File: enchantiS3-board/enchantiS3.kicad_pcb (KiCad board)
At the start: 4 copper layers, 55.9 x 25.4 mm, 60 parts, among them J1 USB_C_Receptacle_USB2.0, SW1 B3U-1000P, SW2 B3U-1000P, U1 USBLC6-2P6, U10 BQ25185DLHR, U3 NCV8187AMT330TAG, U4 NCV8187AMT330TAG, U6 MAX17262REWL+T, U7 LSM6DSV16XTR, U8 IIS2MDCTR

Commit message: added CIRMMT logo to silkscreen
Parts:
- added G***: LOGO, logos:CIRMMT_logo, B.Cu at (135.2, 60.2)
- moved G*** 31.5 mm to (103.9, 51.2)

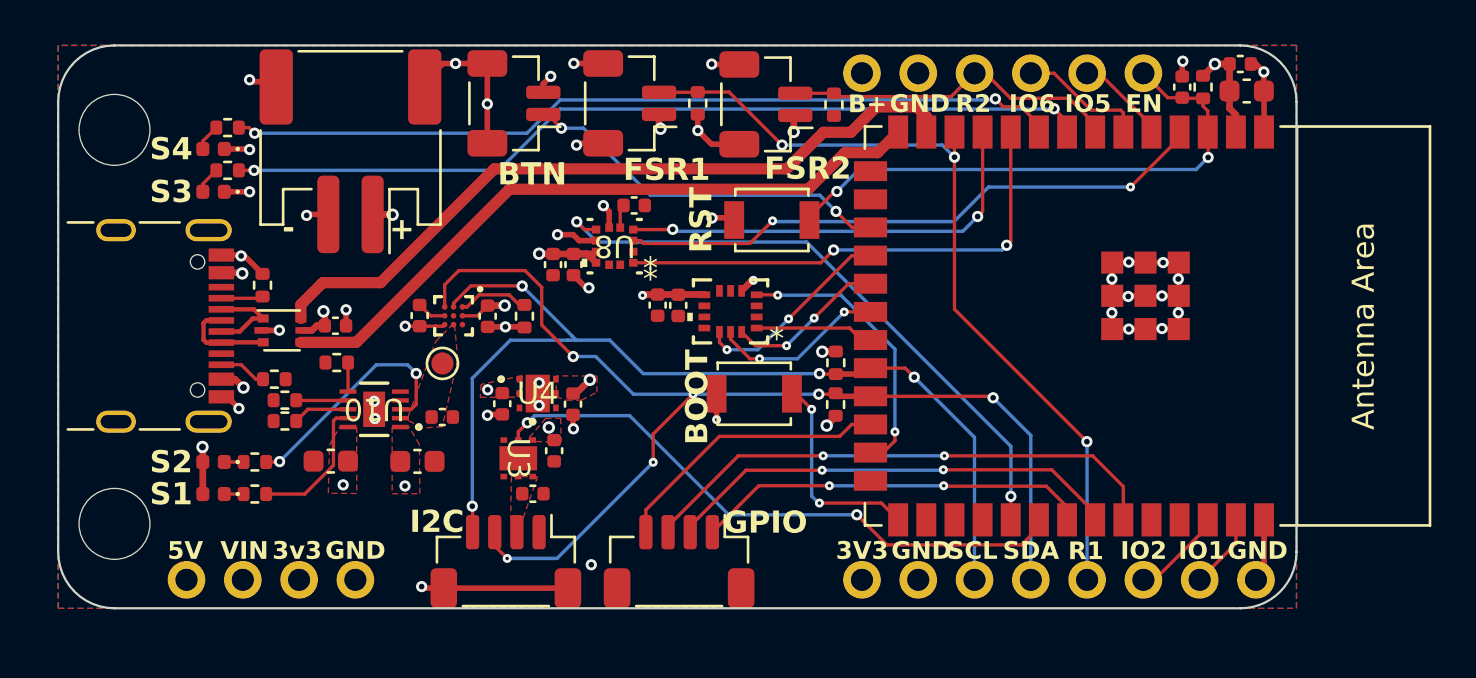
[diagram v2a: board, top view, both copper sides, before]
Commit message: finsished routing for revision 4 of enchantiS3, finished routing for  enchantiS3 Touch
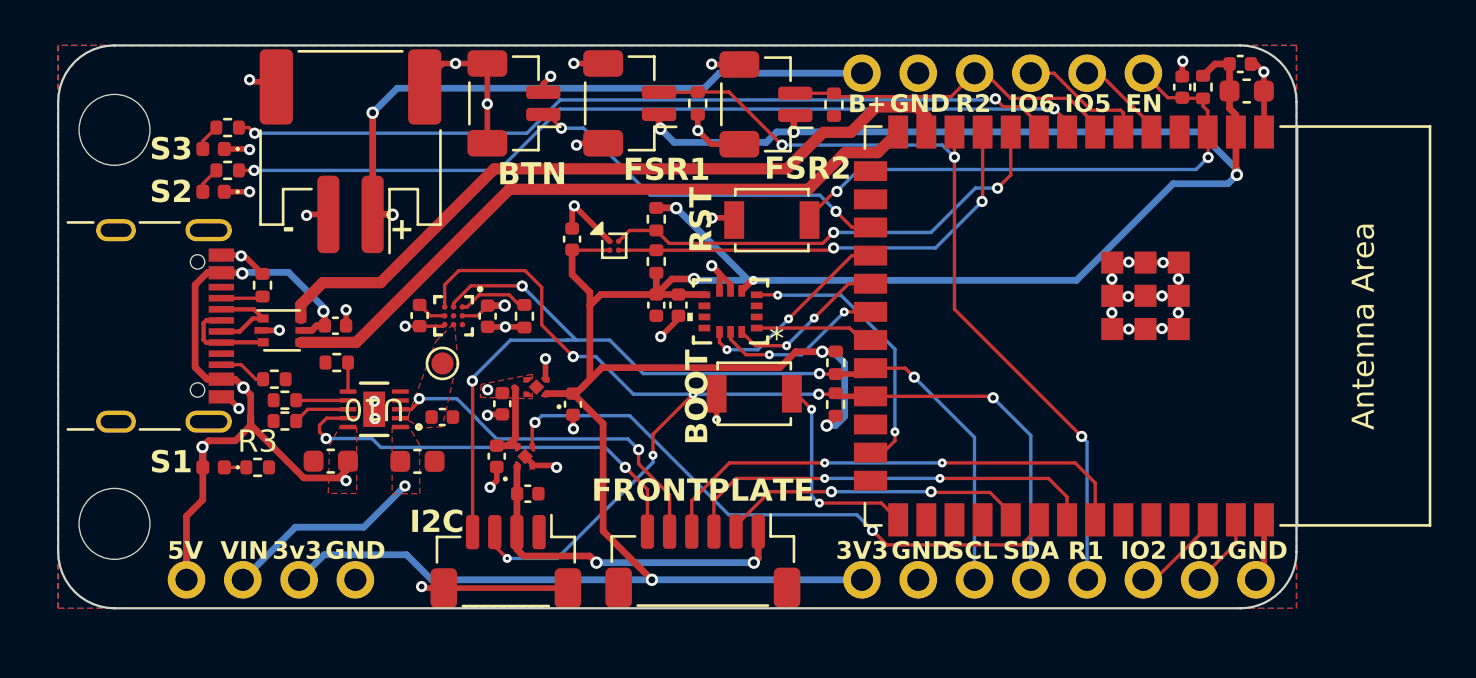
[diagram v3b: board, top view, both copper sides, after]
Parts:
- removed C10: 1uF, Capacitor_SMD:C_0402_1005Metric
- removed C18: 220nF, Capacitor_SMD:C_0402_1005Metric
- removed C7: 0.1uF, Capacitor_SMD:C_0402_1005Metric
- removed CHARGLED2: S2, LED_SMD:LED_0402_1005Metric
- removed R22: 1k, Resistor_SMD:R_0402_1005Metric
- removed TOUCH2: JST-SH-1x04 1.0mm, Connector_JST:JST_SH_BM04B-SRSS-TB_1x04-1MP_P1.00mm_Vertical
- removed U3, U4: NCV8187AMT330TAG, NCV8187-footprints:NCV8187AMT330TAG_ONS-L
- added C3: 220nF, Capacitor_SMD:C_0402_1005Metric, F.Cu at (115.9, 57.0)
- added FP1: JST-SH-1x04 1.0mm, Connector_JST:JST_SH_BM06B-SRSS-TB_1x06-1MP_P1.00mm_Vertical, F.Cu at (121.8, 71.5)
- added R4: 2k2, Resistor_SMD:R_0402_1005Metric, F.Cu at (119.7, 56.1)
- added R9: 2k2, Resistor_SMD:R_0402_1005Metric, F.Cu at (119.7, 58.0)
- added U2: MMC5633NJL, Package_BGA:WLP-4_0.86x0.86mm_P0.4mm, F.Cu at (117.8, 57.3)
- added U5: NCP167AMX330TBG, NCP167AMX330TBG-footprints:XDFN4_1X1_711AJ_ONS, F.Cu at (114.3, 63.7)
- R1, R2: value 1k -> 10k
- R3: value 1k -> 2k2
- U8: value IIS2MDCTR -> NCP167AMX330TBG; footprint IIS2MDCTR-footprints:LGA-12_2X2X0P7_STM -> NCP167AMX330TBG-footprints:XDFN4_1X1_711AJ_ONS
- moved U8 10.3 mm to (113.8, 66.8), turned to 90 degrees
- moved C20 5.95 mm to (120.7, 60.0)
- moved C6 4.16 mm to (119.7, 60.0)
- moved C4 2.60 mm to (112.5, 66.8)
- moved R3 1.21 mm to (101.7, 67.3)
- moved CHARGLED1 1.20 mm to (99.7, 67.3)
- moved C5 0.23 mm to (113.9, 68.5)
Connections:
- MCU1 pad 10: /SPC -> /SCL2
- MCU1 pad 11: /SDIO -> /SDA2
- MCU1 pad 24: /EVT4 -> /LED4
- MCU1 pad 31: /MAG_INT -> /BTN_FP
- MCU1 pad 33: /EVT1 -> /LED1
- MCU1 pad 34: /EVT2 -> /LED2
- MCU1 pad 35: /EVT3 -> /LED3
- MCU1 pad 4: /CS1 -> unconnected-(MCU1-GPIO4/TOUCH4/ADC1_CH3-Pad4)
- R3 pad 2: /STAT1 -> GND
- U8 pad 1: /SPC -> 3V3_AUX
- U8 pad 2: unconnected-(U8-NC-Pad2) -> GND
- U8 pad 3: /CS1 -> /LDO_EN
- U8 pad 4: /SDIO -> SYS
- U8 pad 5: Net-(U8-C1) -> GND
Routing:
- net +3V3: track 15.6 -> 140.4 mm
- net /MAG_INT: track 28.1 -> 0.00 mm, vias 2 -> 0
- net +BATT: track 3.01 -> 30.4 mm, vias 2 -> 3
- net /CS1: track 27.0 -> 0.00 mm, vias 2 -> 0
- net VUSB: track 6.01 -> 32.8 mm
- net /EVT3: track 24.2 -> 0.00 mm, vias 2 -> 0
- net /SPC: track 22.4 -> 0.00 mm, vias 2 -> 0
- net /LED2: track 0.00 -> 22.3 mm, vias 0 -> 2
- net /SCL2: track 0.00 -> 21.4 mm, vias 0 -> 2
- net /EVT2: track 20.7 -> 0.00 mm, vias 2 -> 0
- net /SDA2: track 0.00 -> 20.5 mm, vias 0 -> 2
- net /SDIO: track 19.8 -> 0.00 mm, vias 2 -> 0
- net /LED1: track 0.00 -> 19.1 mm, vias 0 -> 2
- net /EVT1: track 17.9 -> 0.00 mm, vias 2 -> 0
- net 3V3_AUX: track 0.00 -> 16.2 mm, vias 0 -> 2
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- added copper zone on In2.Cu, net GND
- removed copper zone on F.Cu, net +3V3
- removed copper zone on F.Cu, net 3V3_AUX
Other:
- board text added: "FRONTPLATE"
- board text removed: "EVT1 = GPIO40 EVT2 = GPIO41 EVT3 = GPIO42 EVT4 = GPIO47"
- board text removed: "GPIO"
- board text removed: "S4"

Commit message: updated project to kicad 8.0, switched to using enchantiLibrary footprint/symbols, switched connectors to molex picoclasp, updated imu
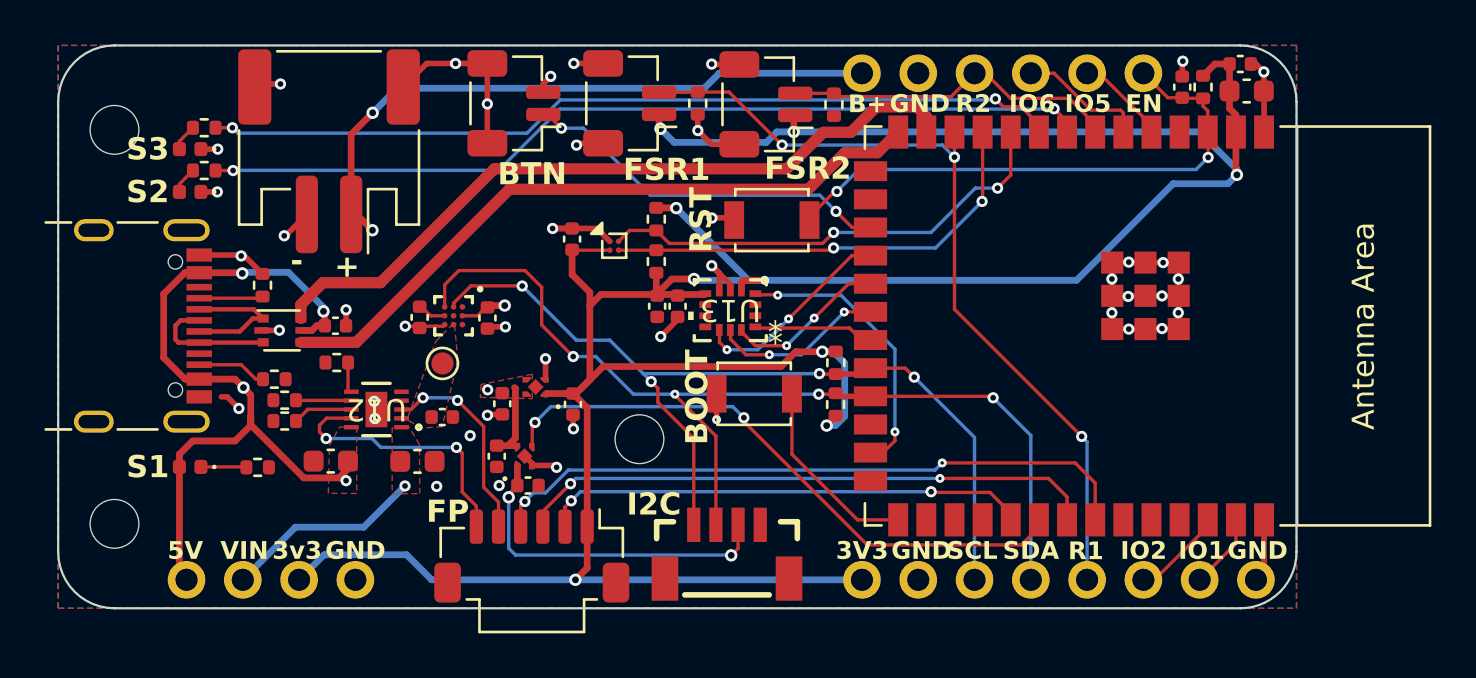
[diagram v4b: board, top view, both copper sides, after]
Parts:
- removed C1, C20: 0.1uF, Capacitor_SMD:C_0402_1005Metric
- removed C2: 0.47uF, Capacitor_SMD:C_0402_1005Metric
- removed C6: 1uF, Capacitor_SMD:C_0402_1005Metric
- removed R14: 10k, Resistor_SMD:R_0402_1005Metric
- removed R19: 0.43k, Resistor_SMD:R_0402_1005Metric
- removed R20: 13k, Resistor_SMD:R_0402_1005Metric
- removed U10: BQ25185DLHR, BQ25185-footprints:WSON10_DLH_TEX-M
- removed U5, U8: NCP167AMX330TBG, NCP167AMX330TBG-footprints:XDFN4_1X1_711AJ_ONS
- removed U6: MAX17262REWL+T, max17262-footprints:21-100221A_W91G1&plus_3_MXM
- removed U7: LSM6DSV16XTR, LSM6DSV16XTR-footprints:LGA14L_LSM6_STM
- added C17: 1uF, Capacitor_SMD:C_0402_1005Metric, F.Cu at (120.7, 60.0)
- added C18: 0.1uF, Capacitor_SMD:C_0402_1005Metric, F.Cu at (119.7, 60.0)
- added C7: 0.1uF, Capacitor_SMD:C_0402_1005Metric, F.Cu at (112.1, 60.6)
- added C8: 0.47uF, Capacitor_SMD:C_0402_1005Metric, F.Cu at (109.0, 60.5)
- added H3: MountingHole, MountingHole:MountingHole_2.2mm_M2, F.Cu at (118.9, 66.0)
- added R11: 13k, Resistor_SMD:R_0402_1005Metric, F.Cu at (102.9, 64.3)
- added R15: 0.3k, Resistor_SMD:R_0402_1005Metric, F.Cu at (102.9, 65.2)
- added U11: MAX17262REWL+T, ENCHANTI_battery-management:MAX17262, F.Cu at (110.5, 60.5)
- added U12: BQ25185DLHR, ENCHANTI_battery-management:WSON10_DLH_TEX, F.Cu at (107.1, 64.7)
- added U13: ICM-42670-P, ENCHANTI_MEMS:LGA14_2P5X3X0P91_TDK, F.Cu at (123.0, 60.2)
- added U4: NCP167AMX330TBG, ENCHANTI_regulators:XDFN4_1X1_711AJ_ONS, F.Cu at (114.3, 63.7)
- added U9: NCP167AMX330TBG, ENCHANTI_regulators:XDFN4_1X1_711AJ_ONS, F.Cu at (113.8, 66.8)
- ANG1, ANG2, ANG3: value JST-SH-1.00mm 1x2 -> CONN HEADER SMD 2POS 1MM; footprint Connector_JST:JST_SH_BM02B-SRSS-TB_1x02-1MP_P1.00mm_Vertical -> ENCHANTI_connectors:Molex_Pico-Clasp_2pin_Vertical
- FP1: value JST-SH-1x04 1.0mm -> CONN HEADER SMD 6POS 1MM; footprint Connector_JST:JST_SH_BM06B-SRSS-TB_1x06-1MP_P1.00mm_Vertical -> ENCHANTI_connectors:Molex_Pico-Clasp_501331-0607_1x06-1MP_P1.00mm_Vertical
- H1, H2: footprint MountingHole:MountingHole_3.2mm_M3_DIN965 -> MountingHole:MountingHole_2.2mm_M2
- TOUCH1: footprint Connector_JST:JST_SH_BM04B-SRSS-TB_1x04-1MP_P1.00mm_Vertical -> ENCHANTI_connectors:JST_SMD_1.0mm-4_Vertical
- moved TOUCH1 9.98 mm to (122.9, 71.4)
- moved FP1 7.72 mm to (114.1, 71.3)
- moved CHARGLED1 1.06 mm to (98.7, 67.3)
- moved R10 1.06 mm to (99.3, 52.0)
- moved R8 1.06 mm to (99.3, 53.9)
- moved STATLED1 1.06 mm to (98.7, 54.9)
- moved STATLED2 1.06 mm to (98.7, 52.9)
- moved J1 1.00 mm to (95.4, 60.9)
- moved BT1 0.97 mm to (104.9, 53.0)
- moved C5 0.37 mm to (113.9, 68.1)
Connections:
- FP1 pad 1: 3V3_AUX -> +3V3
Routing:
- net /BTN_FP: track 14.0 -> 22.0 mm
- net /LED2: track 22.3 -> 29.7 mm
- net /STAT1: track 19.5 -> 12.1 mm
- net /LED1: track 19.1 -> 26.3 mm
- net /SDA: track 52.0 -> 45.0 mm, vias 6 -> 4
- net /STAT2: track 16.3 -> 9.31 mm
- net GND: track 69.8 -> 63.7 mm, vias 42 -> 43
- net /SCL: track 45.8 -> 41.3 mm
- net /THRM: track 3.21 -> 0.00 mm
- net VUSB: track 32.8 -> 34.9 mm, vias 5 -> 4
- net /D-: track 4.19 -> 6.19 mm
- net /D+: track 4.36 -> 5.82 mm
- net Net-(CHARGLED1-K): track 0.99 -> 2.06 mm
- net /BLUELED: track 39.2 -> 40.3 mm
- net /ORANGELED: track 37.7 -> 38.7 mm
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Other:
- board text added: "EnchantiS3 v0.4 2024-10 Albert Niyonsenga"
- board text added: "FP"
- board text removed: "EnchantiS3 v0.4 2024-06 Albert Niyonsenga"
- board text removed: "FRONTPLATE"

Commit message: fixed error in BOM, updated prod files
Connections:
- U11 pad B3: +BATT_SYS -> CHRG+

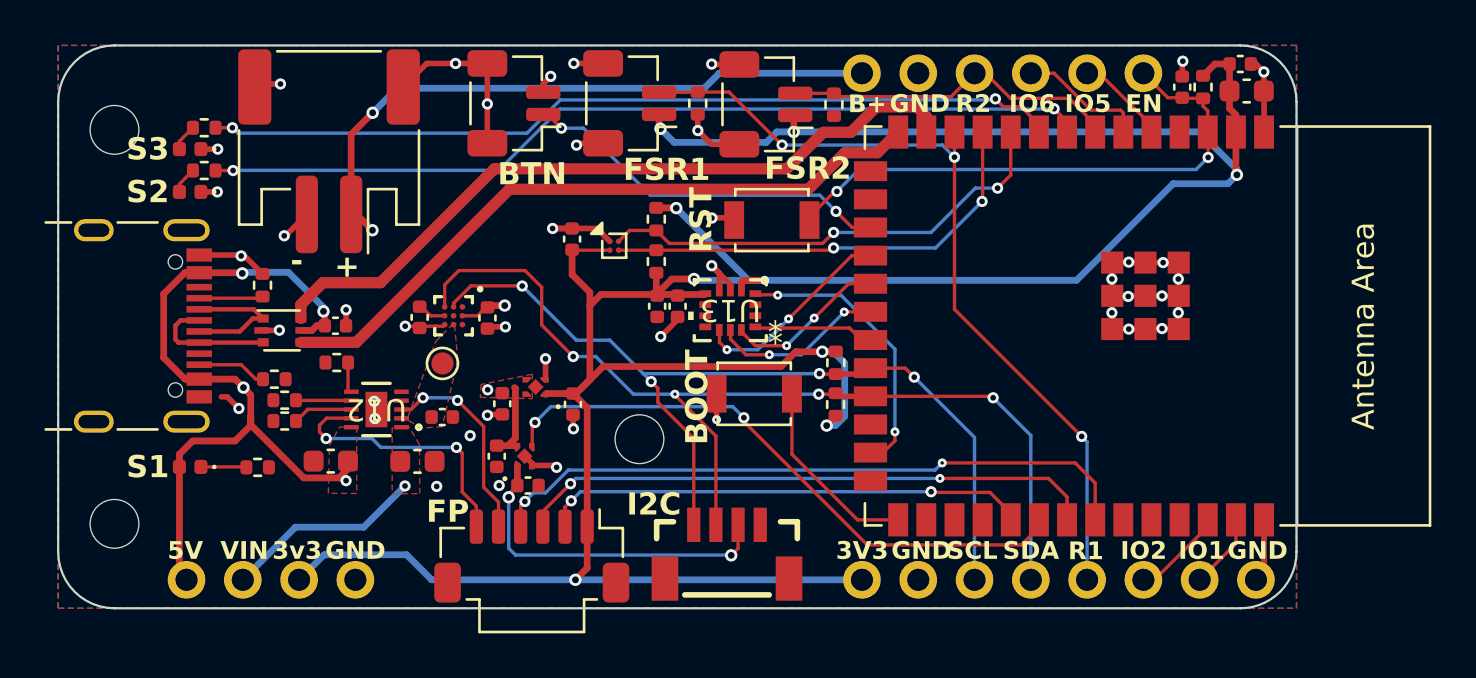
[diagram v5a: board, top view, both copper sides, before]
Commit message: fixed hole size constraints for pcbway manufacturing, updated frontplate connector,
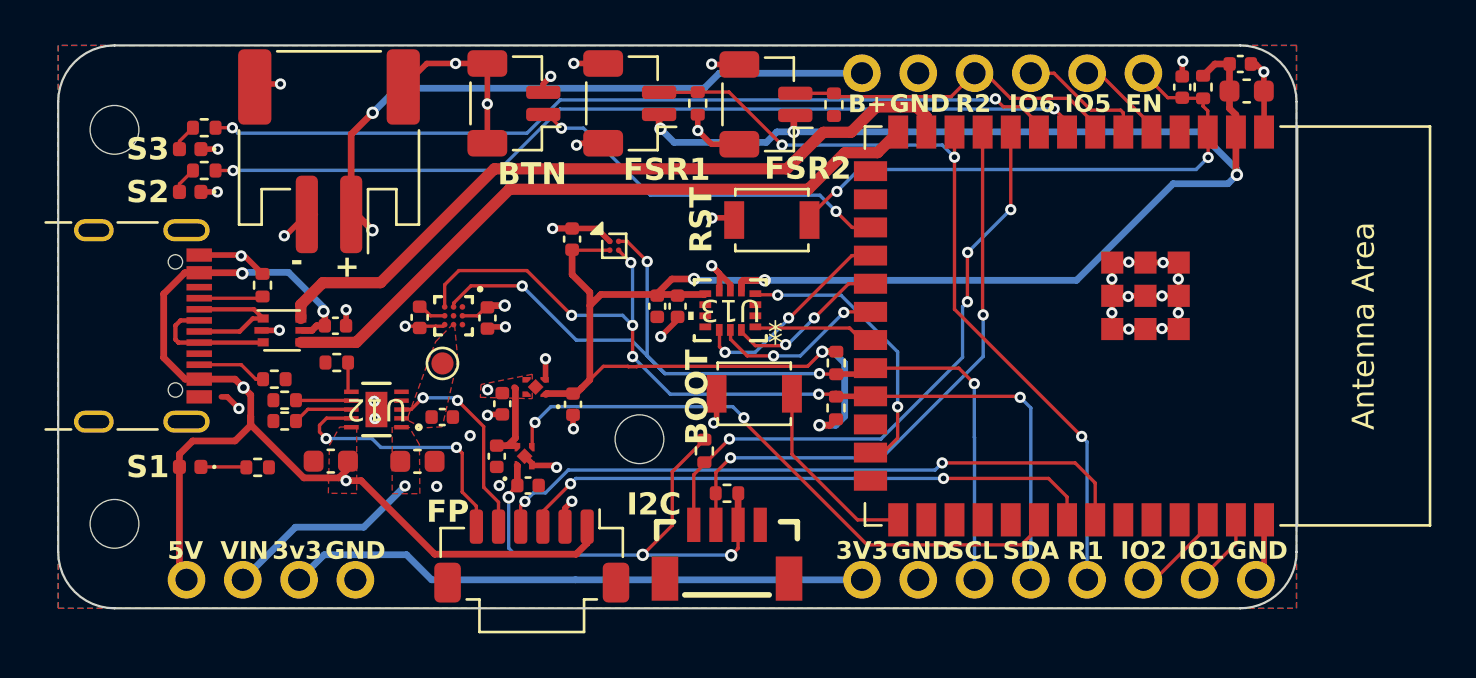
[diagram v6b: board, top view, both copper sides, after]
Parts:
- moved R9 10.5 mm to (127.8, 64.6)
- moved R4 10.4 mm to (127.8, 62.6)
- moved R13 7.14 mm to (121.9, 66.6)
- moved R12 6.33 mm to (122.9, 68.5), turned to 0 degrees
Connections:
- FP1 pad 1: +3V3 -> VUSB
- FP1 pad 2: /BTN_FP -> GND
- R12 pad 1: /SDA -> /SDA2
- R12 pad 2: +3V3 -> 3V3_AUX
- R13 pad 1: /SCL -> /SCL2
- R13 pad 2: +3V3 -> 3V3_AUX
- R4 pad 1: /SCL2 -> /SCL
- R9 pad 1: /SDA2 -> /SDA
- TOUCH1 pad 3: /SDA -> /SDA2
- TOUCH1 pad 4: /SCL -> /SCL2
- U2 pad A2: /SCL2 -> /SCL
- U2 pad B2: /SDA2 -> /SDA
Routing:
- net /BTN_FP: track 22.0 -> 0.00 mm, vias 2 -> 0
- net VUSB: track 34.9 -> 48.2 mm
- net +3V3: track 140.6 -> 132.4 mm, vias 9 -> 7
- net 3V3_AUX: track 15.6 -> 23.4 mm, vias 2 -> 3
- net /SCL2: track 21.4 -> 27.7 mm, vias 2 -> 4
- net /SDA2: track 20.5 -> 26.7 mm
- net /SDA: track 45.0 -> 42.6 mm, vias 4 -> 6
- net GND: track 63.7 -> 65.2 mm, vias 43 -> 44
- net /SCL: track 41.3 -> 42.0 mm
